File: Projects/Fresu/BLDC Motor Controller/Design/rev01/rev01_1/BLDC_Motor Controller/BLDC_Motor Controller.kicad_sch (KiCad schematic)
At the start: 0 parts

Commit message: Update 3
Created flat hierarchy and pages, now just need to define them
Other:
- added sheet Block Diagram (Block Diagram.kicad_sch)
- added sheet CAN BUS (CAN BUS.kicad_sch)
- added sheet FET Driver (FET Driver.kicad_sch)
- added sheet Filters (Filters.kicad_sch)
- added sheet MCU (MCU.kicad_sch)
- added sheet MOSFETS (MOSFETS.kicad_sch)
- added sheet Mechanical (Mechanical.kicad_sch)
- added sheet Overview (Overview.kicad_sch)
- note added: "${TITLE}"
- title: (none) -> ESC_Rev01_1
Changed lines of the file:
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@@
   (paper "A4")
   (title_block
-    (date "15 nov 2012")
+    (title "ESC_Rev01_1")
+    (date "2024-01-06")
+    (rev "rev01_1")
+  )
+  (text "${TITLE}\n" (at 116.84 29.21 0)
+    (effects (font (size 5 5)) (justify left bottom))
+  )
+  (sheet (at 66.04 44.45) (size 33.02 26.67) (fields_autoplaced)
+    (stroke (width 0.1524) (type solid))
+    (fill (color 0 0 0 0.0000))
+    (property "Sheetname" "Block Diagram" (at 66.04 43.7384 0)
+      (effects (font (size 1.27 1.27)) (justify left bottom))
+    )
+    (property "Sheetfile" "Block Diagram.kicad_sch" (at 66.04 71.7046 0)
+      (effects (font (size 1.27 1.27)) (justify left top))
+    )
+    (instances
+      (project "BLDC_Motor Controller"
+        (path "/e63e39d7-6ac0-4ffd-8aa3-1841a4541b55" (page "9"))
+      )
+    )
+  )
+  (sheet (at 26.67 78.74) (size 33.02 26.67) (fields_autoplaced)
+    (stroke (width 0.1524) (type solid))
+    (fill (color 0 0 0 0.0000))
+    (property "Sheetname" "MCU" (at 26.67 78.0284 0)
+      (effects (font (size 1.27 1.27)) (justify left bottom))
+    )
+    (property "Sheetfile" "MCU.kicad_sch" (at 26.67 105.9946 0)
+      (effects (font (size 1.27 1.27)) (justify left top))
+    )
+    (instances
+      (project "BLDC_Motor Controller"
+        (path "/e63e39d7-6ac0-4ffd-8aa3-1841a4541b55" (page "2"))
+      )
+    )
+  )
+  (sheet (at 105.41 78.74) (size 33.02 26.67) (fields_autoplaced)
+    (stroke (width 0.1524) (type solid))
+    (fill (color 0 0 0 0.0000))
+    (property "Sheetname" "MOSFETS" (at 105.41 78.0284 0)
+      (effects (font (size 1.27 1.27)) (justify left bottom))
+    )
+    (property "Sheetfile" "MOSFETS.kicad_sch" (at 105.41 105.9946 0)
+      (effects (font (size 1.27 1.27)) (justify left top))
+    )
+    (instances
+      (project "BLDC_Motor Controller"
+        (path "/e63e39d7-6ac0-4ffd-8aa3-1841a4541b55" (page "4"))
+      )
+    )
+  )
+  (sheet (at 184.15 78.74) (size 33.02 26.67) (fields_autoplaced)
+    (stroke (width 0.1524) (type solid))
+    (fill (color 0 0 0 0.0000))
+    (property "Sheetname" "CAN BUS" (at 184.15 78.0284 0)
+      (effects (font (size 1.27 1.27)) (justify left bottom))
+    )
+    (property "Sheetfile" "CAN BUS.kicad_sch" (at 184.15 105.9946 0)
+      (effects (font (size 1.27 1.27)) (justify left top))
+    )
+    (instances
+      (project "BLDC_Motor Controller"
+        (path "/e63e39d7-6ac0-4ffd-8aa3-1841a4541b55" (page "5"))
+      )
+    )
+  )
+  (sheet (at 66.04 78.74) (size 33.02 26.67) (fields_autoplaced)
+    (stroke (width 0.1524) (type solid))
+    (fill (color 0 0 0 0.0000))
+    (property "Sheetname" "FET Driver" (at 66.04 78.0284 0)
+      (effects (font (size 1.27 1.27)) (justify left bottom))
+    )
+    (property "Sheetfile" "FET Driver.kicad_sch" (at 66.04 105.9946 0)
+      (effects (font (size 1.27 1.27)) (justify left top))
+    )
+    (property "Field2" "" (at 66.04 78.74 0)
+      (effects (font (size 1.27 1.27)) hide)
+    )
+    (instances
+      (project "BLDC_Motor Controller"
+        (path "/e63e39d7-6ac0-4ffd-8aa3-1841a4541b55" (page "3"))
+      )
+    )
+  )
+  (sheet (at 144.78 78.74) (size 33.02 26.67) (fields_autoplaced)
+    (stroke (width 0.1524) (type solid))
+    (fill (color 0 0 0 0.0000))
+    (property "Sheetname" "Filters" (at 144.78 78.0284 0)
+      (effects (font (size 1.27 1.27)) (justify left bottom))
+    )
+    (property "Sheetfile" "Filters.kicad_sch" (at 144.78 105.9946 0)
+      (effects (font (size 1.27 1.27)) (justify left top))
+    )
+    (instances
+      (project "BLDC_Motor Controller"
+        (path "/e63e39d7-6ac0-4ffd-8aa3-1841a4541b55" (page "6"))
+      )
+    )
+  )
+  (sheet (at 26.67 44.45) (size 33.02 26.67) (fields_autoplaced)
+    (stroke (width 0.1524) (type solid))
+    (fill (color 0 0 0 0.0000))
+    (property "Sheetname" "Overview" (at 26.67 43.7384 0)
+      (effects (font (size 1.27 1.27)) (justify left bottom))
+    )
+    (property "Sheetfile" "Overview.kicad_sch" (at 26.67 71.7046 0)
+      (effects (font (size 1.27 1.27)) (justify left top))
+    )
+    (instances
+      (project "BLDC_Motor Controller"
+        (path "/e63e39d7-6ac0-4ffd-8aa3-1841a4541b55" (page "8"))
+      )
+    )
+  )
+  (sheet (at 26.67 113.03) (size 33.02 26.67) (fields_autoplaced)
+    (stroke (width 0.1524) (type solid))
+    (fill (color 0 0 0 0.0000))
+    (property "Sheetname" "Mechanical" (at 26.67 112.3184 0)
+      (effects (font (size 1.27 1.27)) (justify left bottom))
+    )
+    (property "Sheetfile" "Mechanical.kicad_sch" (at 26.67 140.2846 0)
+      (effects (font (size 1.27 1.27)) (justify left top))
+    )
+    (instances
+      (project "BLDC_Motor Controller"
+        (path "/e63e39d7-6ac0-4ffd-8aa3-1841a4541b55" (page "7"))
+      )
+    )
   )
   (sheet_instances

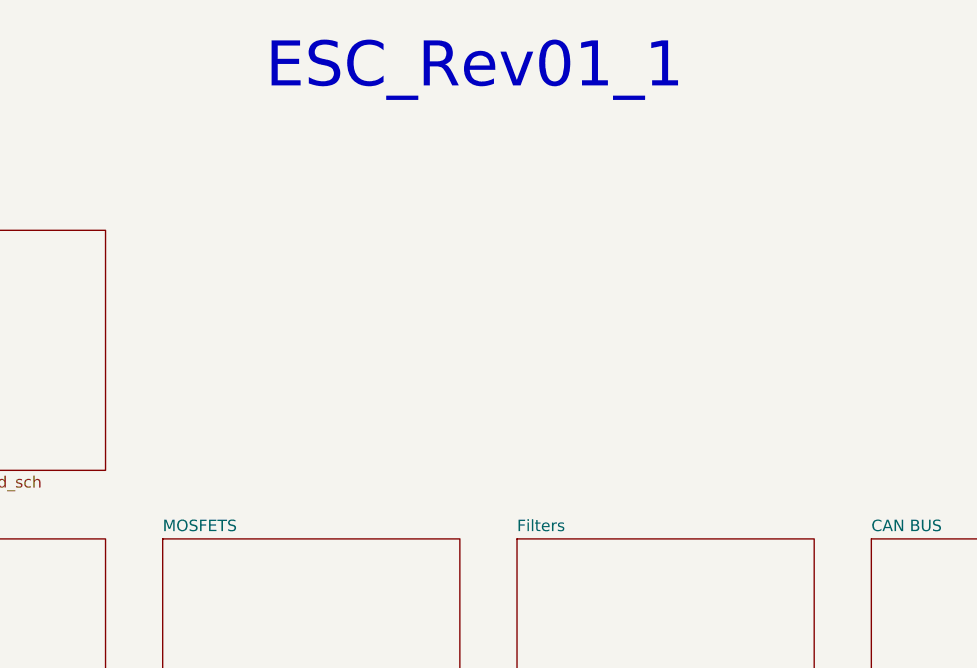
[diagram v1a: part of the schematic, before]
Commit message: UPDATE 10
COMPELTED STEP-DOWN SCHEMATAIC
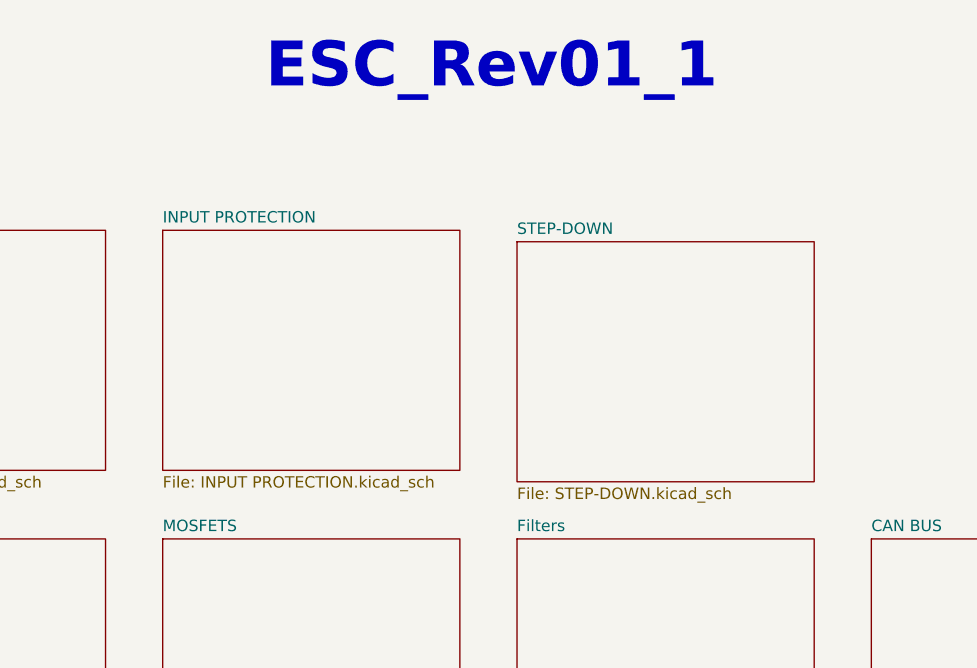
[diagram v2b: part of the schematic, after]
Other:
- added sheet INPUT PROTECTION (INPUT PROTECTION.kicad_sch)
- added sheet STEP-DOWN (STEP-DOWN.kicad_sch)
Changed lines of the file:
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@@
   )
   (text "${TITLE}\n" (at 116.84 29.21 0)
-    (effects (font (size 5 5)) (justify left bottom))
+    (effects (font (size 5 5) (thickness 1) bold) (justify left bottom))
+  )
+  (sheet (at 105.41 44.45) (size 33.02 26.67) (fields_autoplaced)
+    (stroke (width 0.1524) (type solid))
+    (fill (color 0 0 0 0.0000))
+    (property "Sheetname" "INPUT PROTECTION" (at 105.41 43.7384 0)
+      (effects (font (size 1.27 1.27)) (justify left bottom))
+    )
+    (property "Sheetfile" "INPUT PROTECTION.kicad_sch" (at 105.41 71.7046 0)
+      (effects (font (size 1.27 1.27)) (justify left top))
+    )
+    (instances
+      (project "BLDC_Motor Controller"
+        (path "/e63e39d7-6ac0-4ffd-8aa3-1841a4541b55" (page "10"))
+      )
+    )
   )
   (sheet (at 66.04 44.45) (size 33.02 26.67) (fields_autoplaced)
@@
       )
     )
+  )
+  (sheet (at 144.78 45.72) (size 33.02 26.67) (fields_autoplaced)
+    (stroke (width 0.1524) (type solid))
+    (fill (color 0 0 0 0.0000))
+    (property "Sheetname" "STEP-DOWN" (at 144.78 45.0084 0)
+      (effects (font (size 1.27 1.27)) (justify left bottom))
+    )
+    (property "Sheetfile" "STEP-DOWN.kicad_sch" (at 144.78 72.9746 0)
+      (effects (font (size 1.27 1.27)) (justify left top))
+    )
+    (instances
+      (project "BLDC_Motor Controller"
+        (path "/e63e39d7-6ac0-4ffd-8aa3-1841a4541b55" (page "11"))
+      )
+    )

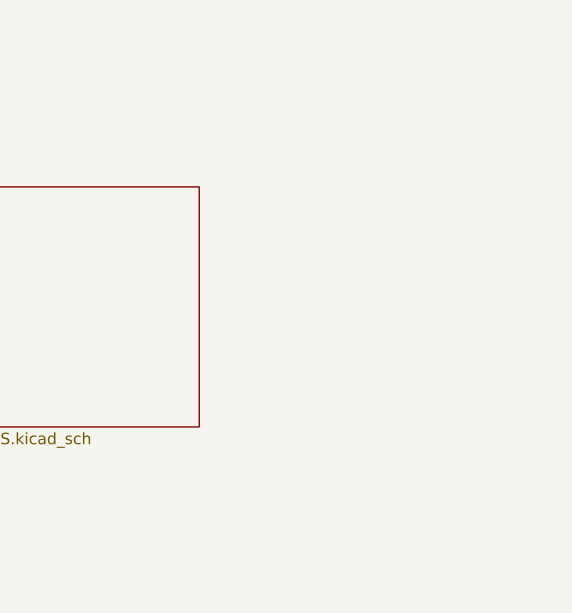
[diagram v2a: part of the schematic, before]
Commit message: Update 13
Added:
1) USB Schematic
2) footprints to all parts
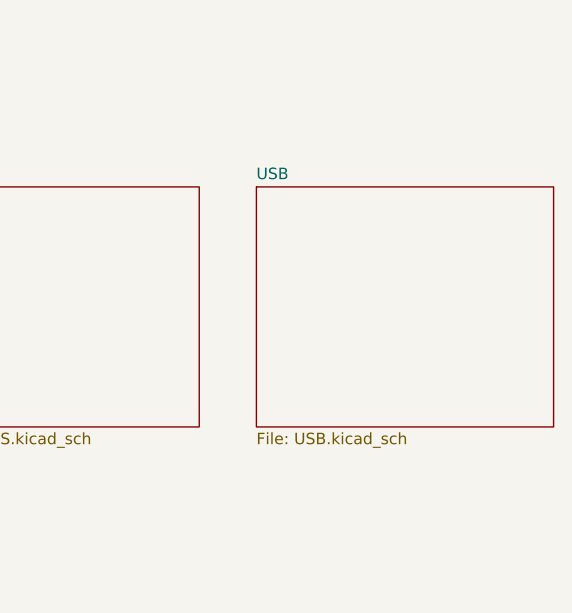
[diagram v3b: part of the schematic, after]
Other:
- added sheet USB (USB.kicad_sch)
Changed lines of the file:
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@@
+    )
+  )
+  (sheet (at 223.52 78.74) (size 33.02 26.67) (fields_autoplaced)
+    (stroke (width 0.1524) (type solid))
+    (fill (color 0 0 0 0.0000))
+    (property "Sheetname" "USB" (at 223.52 78.0284 0)
+      (effects (font (size 1.27 1.27)) (justify left bottom))
+    )
+    (property "Sheetfile" "USB.kicad_sch" (at 223.52 105.9946 0)
+      (effects (font (size 1.27 1.27)) (justify left top))
+    )
+    (instances
+      (project "BLDC_Motor Controller"
+        (path "/e63e39d7-6ac0-4ffd-8aa3-1841a4541b55" (page "12"))
+      )
     )
   )
